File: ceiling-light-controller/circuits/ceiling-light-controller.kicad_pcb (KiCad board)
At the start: 2 copper layers, 90.5 x 83 mm, 18 parts, among them J1 Screw_Terminal_01x03, J2 Screw_Terminal_01x02, Q1 BT136-500, U1 LTV-817, U2 HLK-PM03, U3 MOC3021M, U4 WeMos_mini

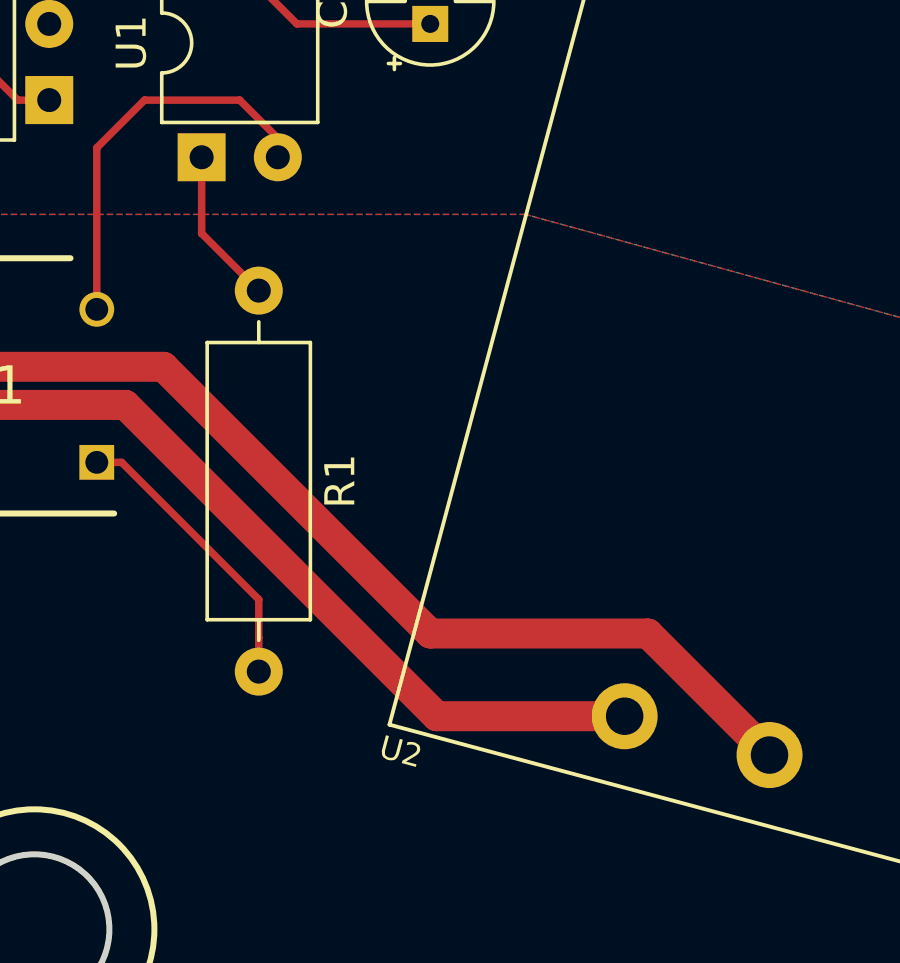
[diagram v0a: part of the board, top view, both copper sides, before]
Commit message: fixing submodule path once again
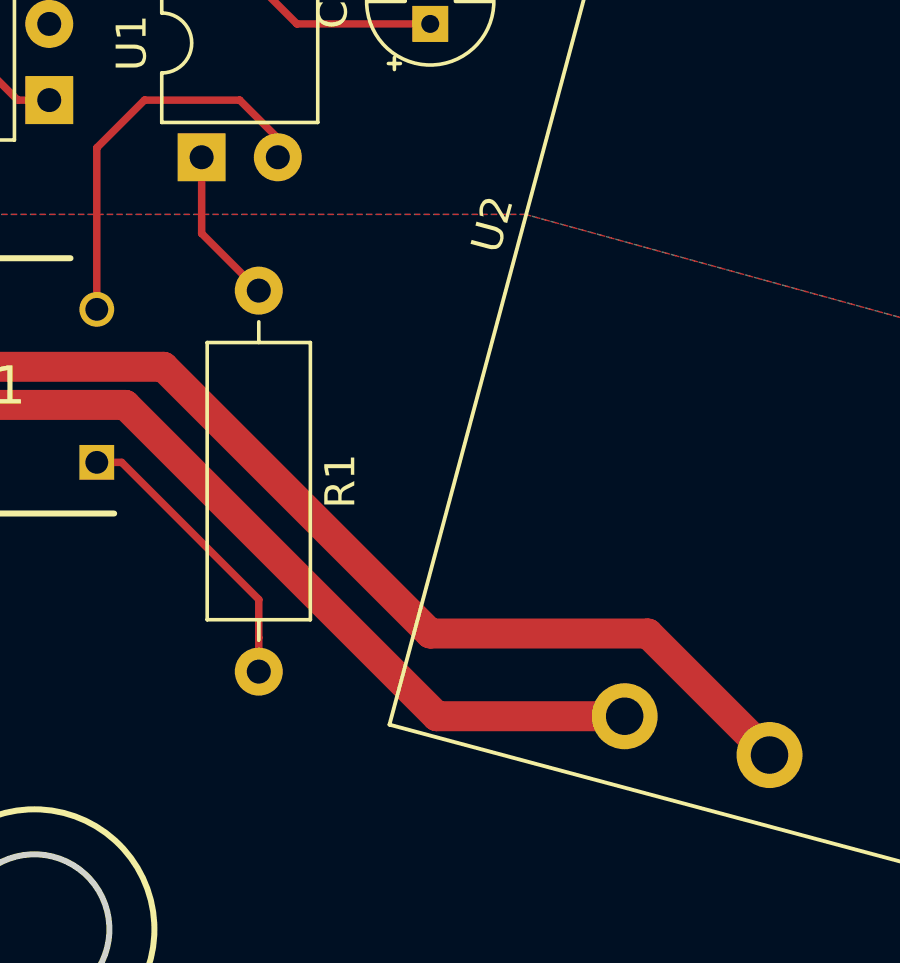
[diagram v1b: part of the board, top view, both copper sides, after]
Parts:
- U2: value HLK-PM03 -> HLK-PM05; footprint Power_Supply:HLK-PM01 -> Power_Supply:HLK-PM05
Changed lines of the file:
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@@
     (add_net "Net-(U4-Pad9)")
+  )
+  (module Power_Supply:HLK-PM05 locked (layer F.Cu)
+    (at 172.72 105.41 75)
+    (fp_text reference U2 (at 0 -11 75) (layer F.SilkS)
+      (effects (font (size 1 1) (thickness 0.15)))
+    )
+    (fp_text value HLK-PM05 (at 0 11 75) (layer F.Fab)
+      (effects (font (size 1 1) (thickness 0.15)))
+    )
+    (fp_line (start 17 10) (end 17 -10) (layer F.SilkS) (width 0.127))
+    (fp_line (start -17 -10) (end -17 10) (layer F.SilkS) (width 0.127))
+    (fp_line (start -17 10) (end 17 10) (layer F.SilkS) (width 0.127))
+    (fp_line (start 17 -10) (end -17 -10) (layer F.SilkS) (width 0.127))
+    (pad 1 thru_hole circle (at -14.7 -2.5 75) (size 2.2 2.2) (drill 1.25) (layers *.Cu *.Mask F.SilkS)
+      (net 25 "Net-(BR1-Pad4)"))
+    (pad 2 thru_hole circle (at -14.7 2.5 75) (size 2.2 2.2) (drill 1.25) (layers *.Cu *.Mask F.SilkS)
+      (net 23 "Net-(J1-Pad1)"))
+    (pad 3 thru_hole circle (at 14.7 -7.7 75) (size 2.2 2.2) (drill 1.25) (layers *.Cu *.Mask F.SilkS)
+      (net 1 GND))
+    (pad 4 thru_hole circle (at 14.7 7.7 75) (size 2.2 2.2) (drill 1.25) (layers *.Cu *.Mask F.SilkS)
+      (net 26 "Net-(D1-Pad1)"))
+    (model C:/Engineering/KiCAD_Libraries/3D/Power_Supplies/AC_DC_Converters/VRML/HiLink_HLK-PM03.wrl
+      (at (xyz 0 0 0))
+      (scale (xyz 1 1 1))
+      (rotate (xyz 0 0 0))
+    )
   )
   (module Package_DIP:DIP-6_W7.62mm (layer F.Cu)
@@
       (effects (font (size 1 1) (thickness 0.15)))
     )
-    (pad 2 thru_hole circle (at 5.08 0 45) (size 3 3) (drill 1.52) (layers *.Cu *.Mask)
+    (pad 2 thru_hole circle (at 5.079999 0 45) (size 3 3) (drill 1.52) (layers *.Cu *.Mask)
       (net 22 "Net-(C5-Pad2)"))
     (pad 1 thru_hole rect (at 0 0 45) (size 3 3) (drill 1.52) (layers *.Cu *.Mask)
@@
     )
   )
-  (module Power_Supply:HLK-PM01 locked (layer F.Cu)
-    (at 172.72 105.41 75)
-    (fp_text reference U2 (at -17.78 -9.398 165) (layer F.SilkS)
-      (effects (font (size 0.762 0.762) (thickness 0.127)))
-    )
-    (fp_text value HLK-PM03 (at 0 11 75) (layer F.Fab)
-      (effects (font (size 0.762 0.762) (thickness 0.127)))
-    )
-    (fp_line (start 17 -10) (end -17 -10) (layer F.SilkS) (width 0.127))
-    (fp_line (start -17 10) (end 17 10) (layer F.SilkS) (width 0.127))
-    (fp_line (start -17 -10) (end -17 10) (layer F.SilkS) (width 0.127))
-    (fp_line (start 17 10) (end 17 -10) (layer F.SilkS) (width 0.127))
-    (pad 4 thru_hole circle (at 14.7 7.7 75) (size 2.2 2.2) (drill 1.25) (layers *.Cu *.Mask)
-      (net 26 "Net-(D1-Pad1)"))
-    (pad 3 thru_hole circle (at 14.7 -7.7 75) (size 2.2 2.2) (drill 1.25) (layers *.Cu *.Mask)
-      (net 1 GND))
-    (pad 2 thru_hole circle (at -14.7 2.5 75) (size 2.2 2.2) (drill 1.25) (layers *.Cu *.Mask)
-      (net 23 "Net-(J1-Pad1)"))
-    (pad 1 thru_hole circle (at -14.7 -2.5 75) (size 2.2 2.2) (drill 1.25) (layers *.Cu *.Mask)
-      (net 25 "Net-(BR1-Pad4)"))
-    (model C:/Engineering/KiCAD_Libraries/3D/Power_Supplies/AC_DC_Converters/VRML/HLK-PM01.wrl
-      (at (xyz 0 0 0))
-      (scale (xyz 1 1 1))
-      (rotate (xyz 0 0 0))
-    )
-  )

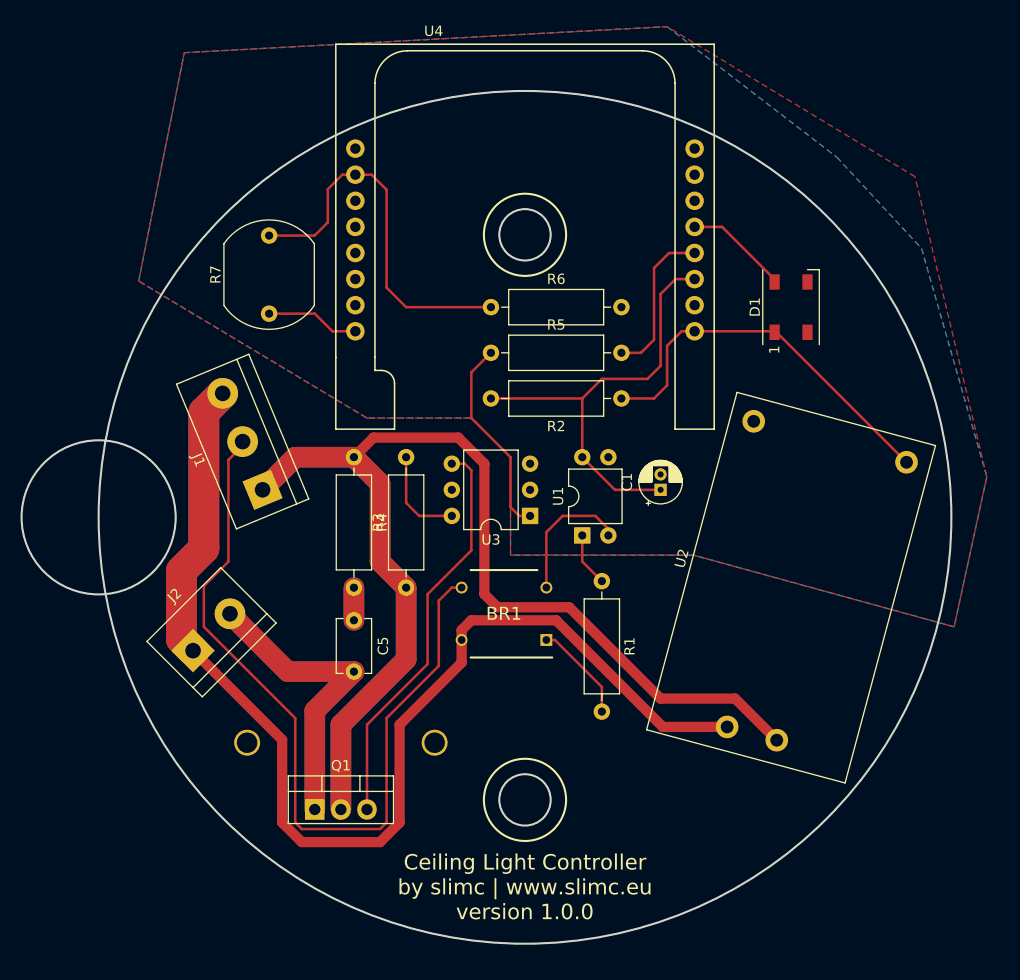
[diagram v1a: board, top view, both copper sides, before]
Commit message: update to PCB layput
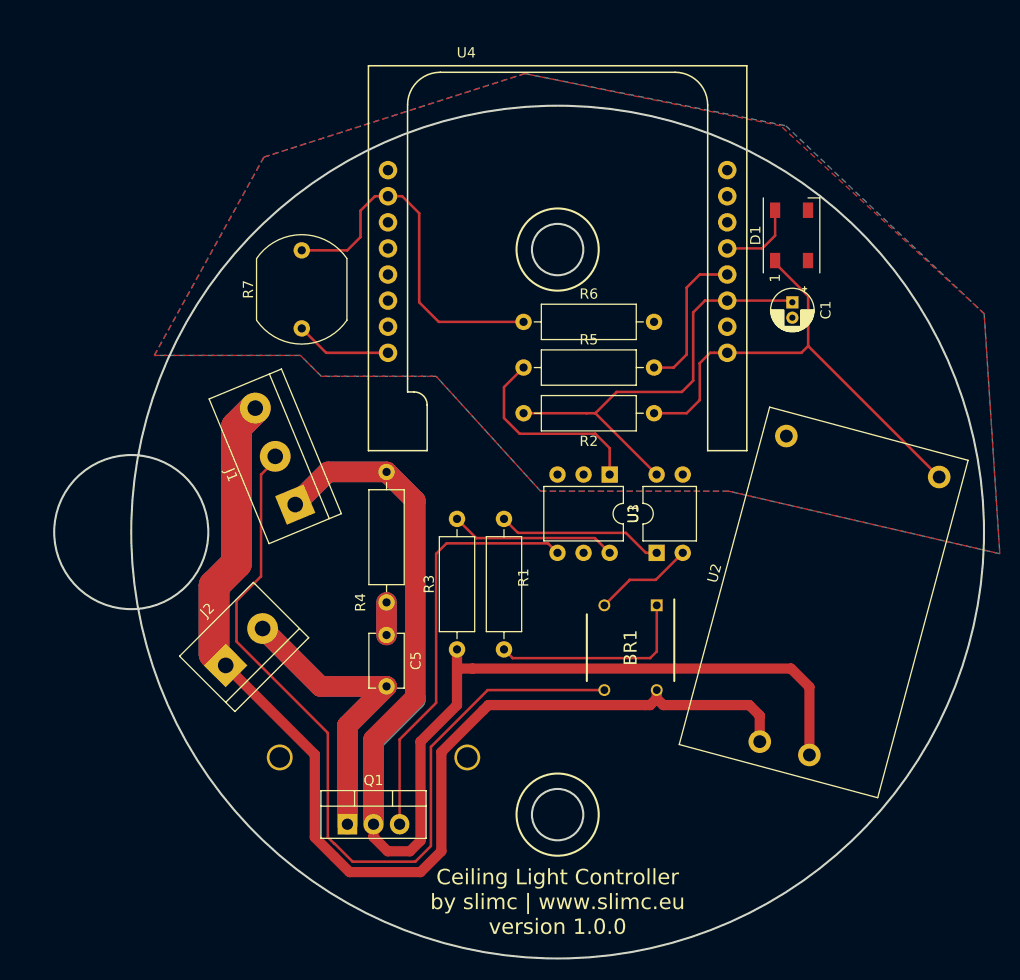
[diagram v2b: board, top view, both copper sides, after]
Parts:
- moved C1 22.3 mm to (172.8, 77.6), turned to 270 degrees
- moved BR1 12.8 mm to (157.1, 111.3), turned to 270 degrees
- moved R1 11.3 mm to (144.8, 98.7)
- moved U3 8.73 mm to (155.1, 94.4), turned to 270 degrees
- moved R3 7.79 mm to (140.2, 111.4)
- moved U1 7.43 mm to (159.6, 102.0)
- moved D1 6.98 mm to (172.8, 71.1)
- moved U4 3.80 mm to (150.0, 73.7)
- moved R5 3.48 mm to (146.7, 84.0)
- moved R6 3.48 mm to (146.7, 79.5)
- moved U2 3.48 mm to (175.9, 106.8)
- moved J2 3.48 mm to (117.7, 113.0)
- moved Q1 3.48 mm to (129.5, 128.4)
- moved R7 3.48 mm to (125.1, 80.2)
- moved J1 3.48 mm to (124.5, 97.3)
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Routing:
- net Net-(R1-Pad1): track 5.23 -> 16.2 mm
- net Net-(BR1-Pad1): track 9.70 -> 20.0 mm
- net Net-(D1-Pad1): track 38.0 -> 47.5 mm
- net Net-(R3-Pad2): track 9.42 -> 16.2 mm
- net Net-(BR1-Pad3): track 78.0 -> 82.6 mm
- net Net-(BR1-Pad2): track 13.2 -> 9.77 mm
- net Net-(J1-Pad1): track 160.0 -> 163.5 mm
- net Net-(BR1-Pad4): track 142.0 -> 138.6 mm
- net Net-(D1-Pad4): track 10.2 -> 7.65 mm
- net Net-(R6-Pad1): track 36.9 -> 35.4 mm
- net Net-(Q1-Pad3): track 39.4 -> 40.4 mm
- net Net-(R5-Pad2): track 15.2 -> 14.7 mm
